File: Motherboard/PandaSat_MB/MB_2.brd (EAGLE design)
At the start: 93.9 x 89.2 mm, 165 parts, among them J1 503182-1852, J2 10118194-0001LF, J3 DCJ0303, J4 BU-SMA-V, J5 BK-18650, K4 PE014006, Q1 IRLML2803, Q2 IRLML2803, Q3 IRLML2803, Q4 IRLML2803, Q5 MOSFET-PCHANNEL-SOIC8SOIC8, Q6 MOSFET-PCHANNEL-SOIC8SOIC8, Q7 MOSFET-PCHANNEL-SOIC8SOIC8, Q8 2N5088, U1 MAX706R, U10 DRV8848, U11 DRV8848, U2 LTC4121-4.2, U3 LSM9DS1, U4 MAX4372TEUK+T, U5 RFM23BP, U6 TPS54226PWPRPWP14_2P31X2P46-L, U7 ATSAMD51, U8 OKL-T3-W12

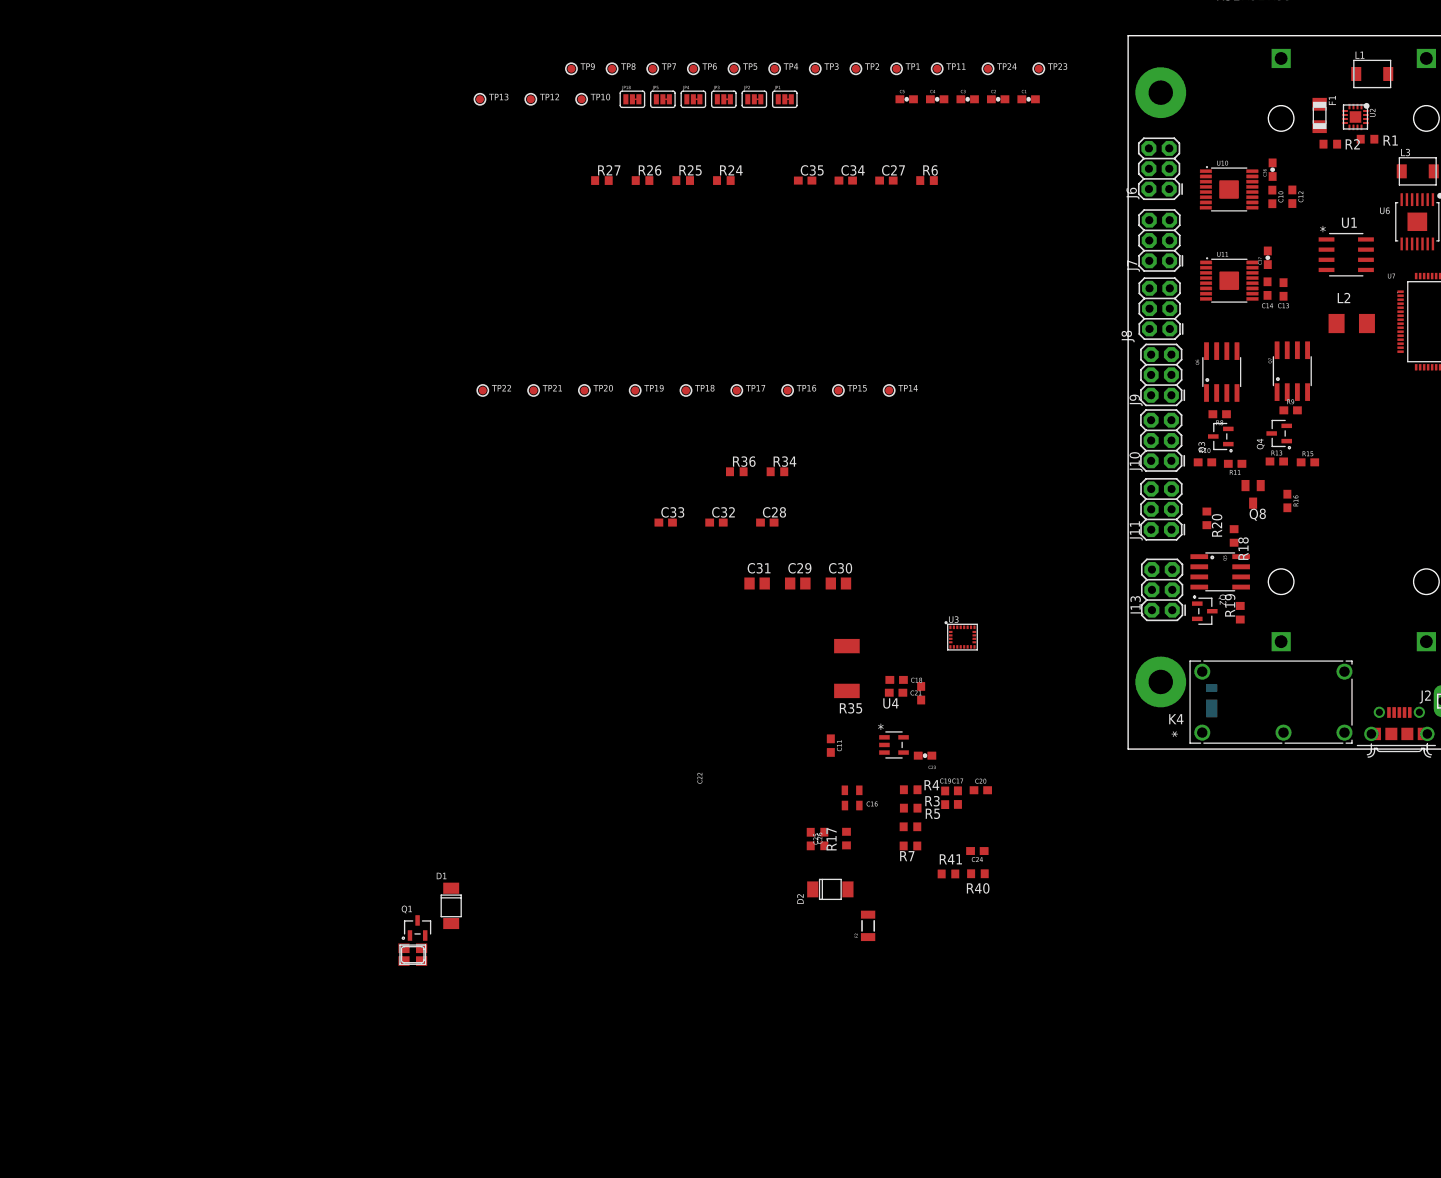
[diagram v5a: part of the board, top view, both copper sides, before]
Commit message: Changed all caps to 0603, need to change to all same part so text size is consistent
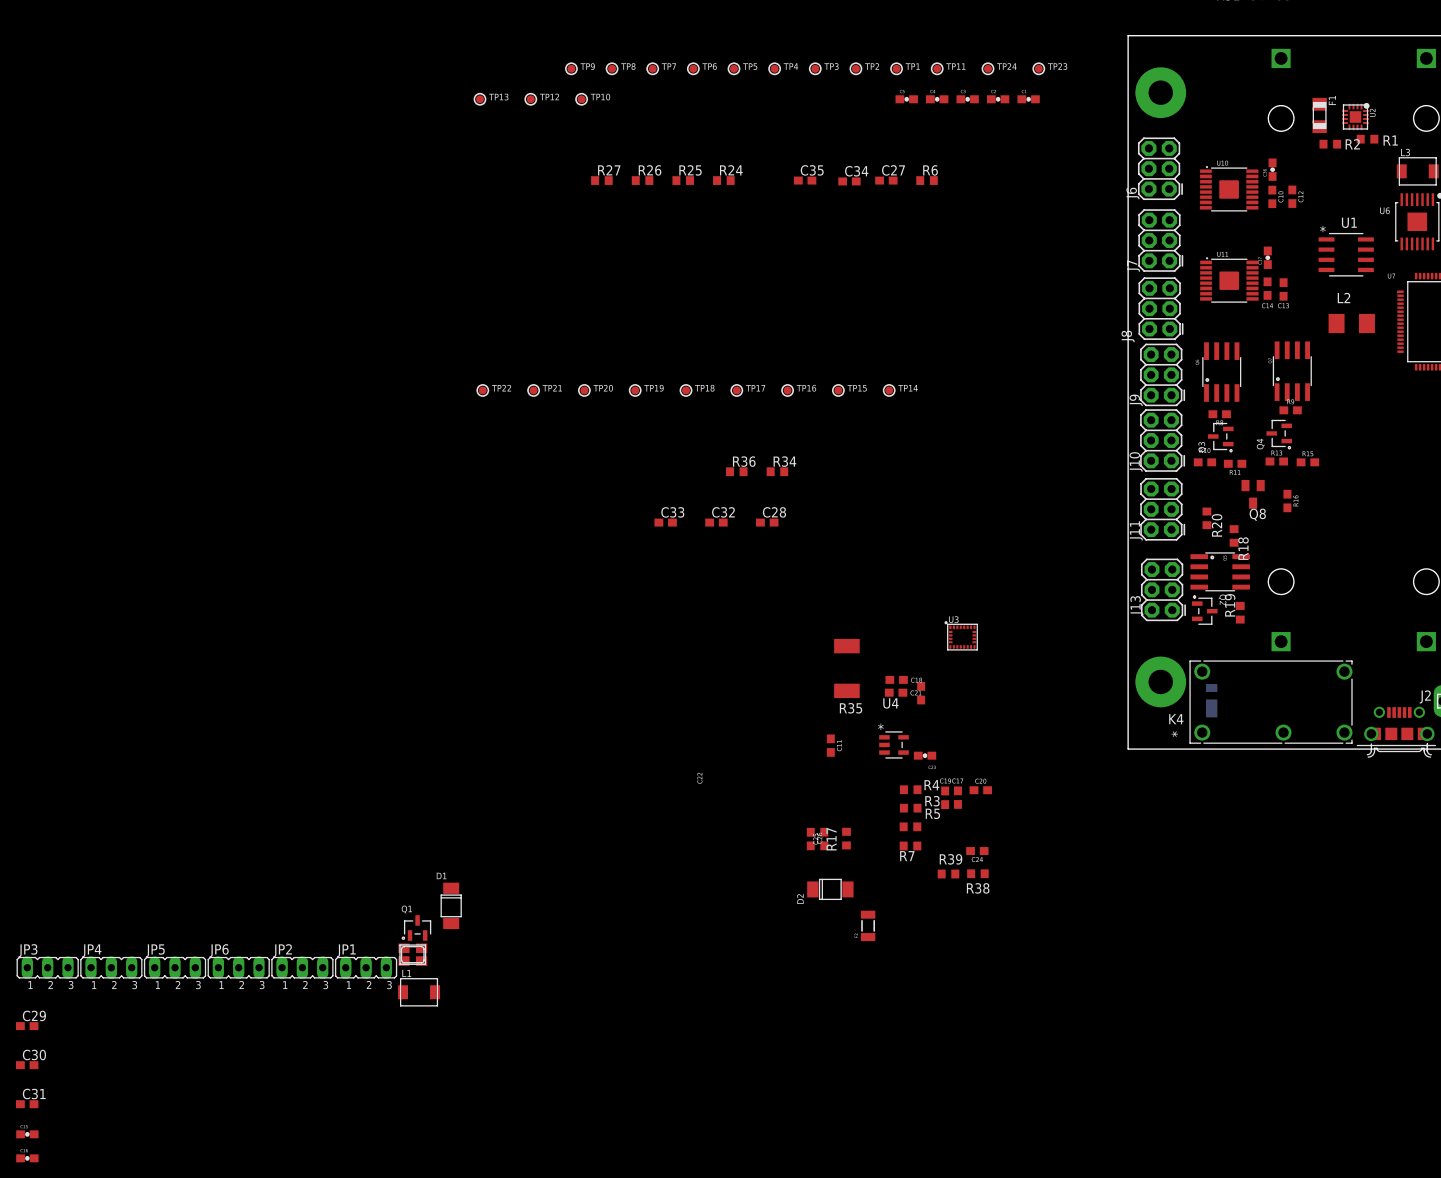
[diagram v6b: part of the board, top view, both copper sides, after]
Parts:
- removed JP18: (no value), SparkFun-Passives:PAD-JUMPER-3-2OF3_NC_BY_TRACE_YES_SILK_FULL_BOX
- added JP6: (no value), jumper:JP2
- C15, C16: device SparkFun-Capacitors:0805 -> SparkFun-Capacitors:0603-CAP
- C29, C30, C31: device resistor:C0805 -> resistor:C0603
- JP1, JP2, JP3, JP4, JP5: device SparkFun-Passives:PAD-JUMPER-3-2OF3_NC_BY_TRACE_YES_SILK_FULL_BOX -> jumper:JP2
- L1: value 56uH -> (none)
- moved L1 165.4 mm to (-183.5, -29.9)
- moved JP3 137.6 mm to (-229.9, -26.8)
- moved JP4 130.7 mm to (-222.0, -26.8)
- moved JP5 124.5 mm to (-214.0, -26.8)
- moved JP2 122.4 mm to (-198.1, -26.8)
- moved JP1 120.5 mm to (-190.1, -26.8)
- moved C30 117.9 mm to (-232.5, -39.0)
- moved C16 112.1 mm to (-232.5, -50.7)
- moved C31 112.1 mm to (-232.5, -43.9)
- moved C15 111.7 mm to (-232.5, -47.7)
- moved C29 111.1 mm to (-232.5, -34.1)
- moved C34 0.47 mm to (-129.7, 71.5)
- renumbered R40 to R38, R41 to R39
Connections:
- removed net I2C_SDOA/G: JP2.2, U3.5
- new net N$57: JP5.2, U3.5
- net !RESET: now also C29.2, JP2.3; no longer C29.1, JP5.3
- net 3.3V: now also JP3.1, JP4.1, JP5.1, JP6.1; no longer JP18.3, JP2.3, JP3.3, JP4.3
- net GND: now also C29.1, C30.1, C31.1, JP3.3, JP4.3, JP5.3, JP6.3; no longer C29.2, C30.2, C31.2, JP18.1, JP2.1, JP3.1, JP4.1
- net N$1: now also JP2.1, U1.7; no longer JP5.2, U1.8
- net N$21: now also JP6.2; no longer JP1.2
- net N$23: now also JP4.2; no longer JP3.2
- net N$26: now also JP3.2; no longer JP4.2
- net N$43: now also C30.2, C31.2; no longer C30.1, C31.1
- net N$5: now also JP2.2, U1.8; no longer JP5.1, U1.7
- net N$8: now also JP1.2; no longer JP18.2
